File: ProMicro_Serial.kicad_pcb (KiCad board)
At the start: 2 copper layers, 17.8 x 33 mm, 41 parts, among them J1 USB_C_Receptacle_USB2.0, J2 Conn_01x06, U1 FT232H

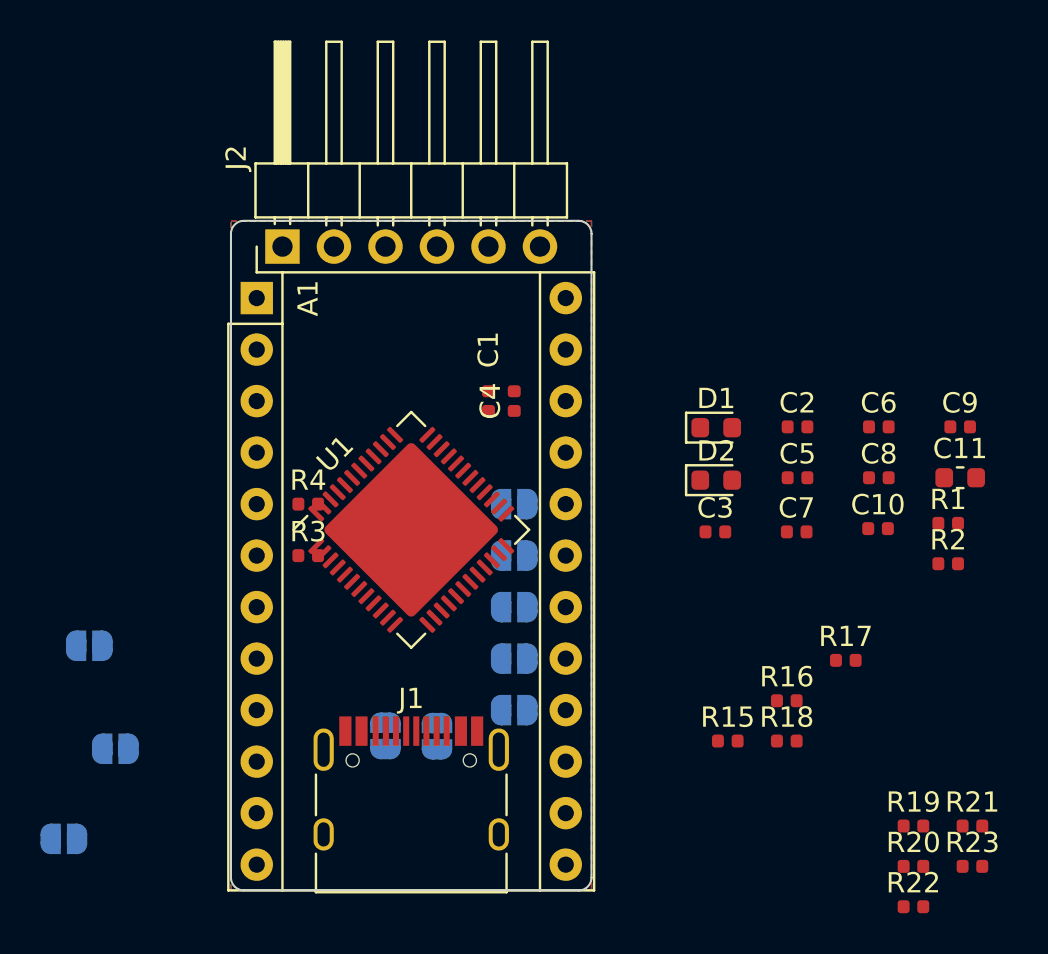
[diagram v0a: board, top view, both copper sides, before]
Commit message: schematic, placed parts
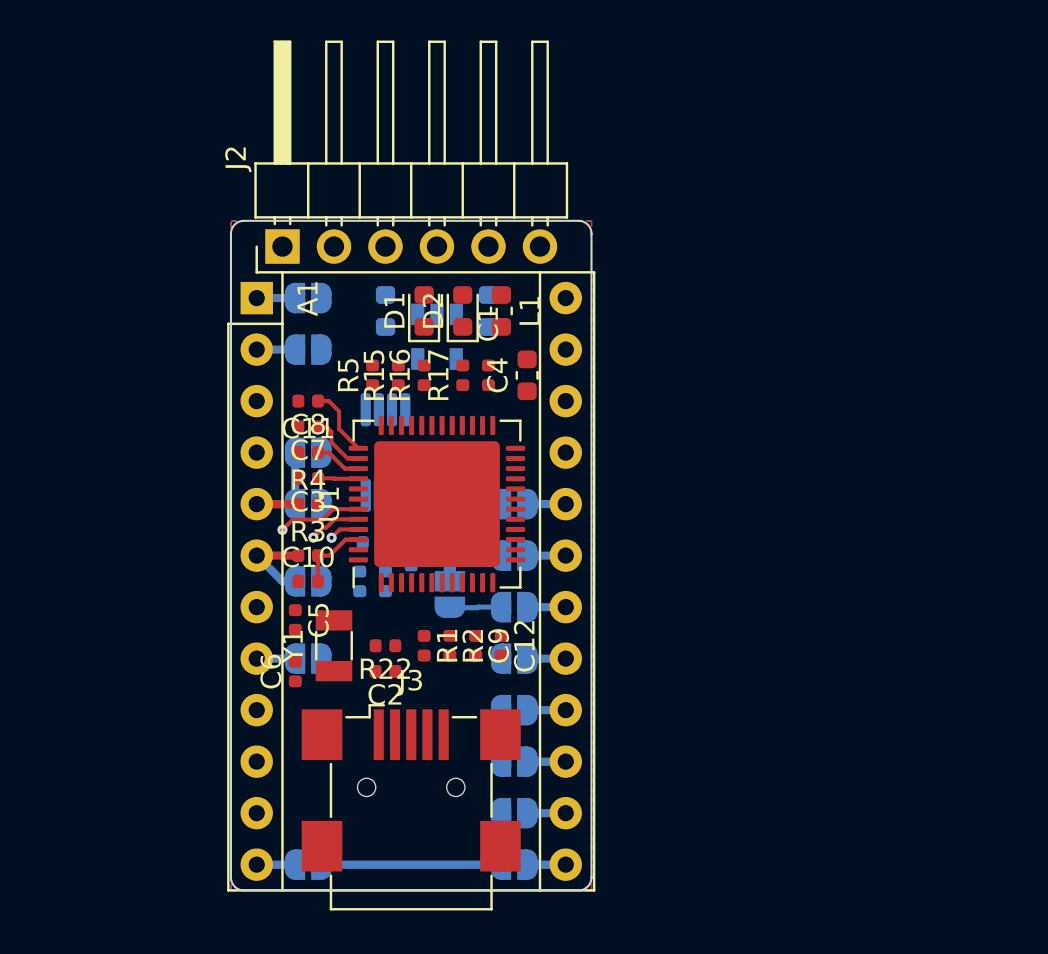
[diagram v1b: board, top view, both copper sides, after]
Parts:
- removed J1: USB_C_Receptacle_USB2.0, Connector_USB:USB_C_Receptacle_HRO_TYPE-C-31-M-12
- removed R18: 4k7, Resistor_SMD:R_0402_1005Metric
- added C12: 100n, Capacitor_SMD:C_0402_1005Metric, F.Cu at (113.7, 93.3)
- added C13: 1µ, Capacitor_SMD:C_0603_1608Metric, B.Cu at (113.0, 76.8)
- added C14: 100n, Capacitor_SMD:C_0603_1608Metric, B.Cu at (108.0, 76.8)
- added J3: USB_B_Mini, Connector_USB:USB_Mini-B_Wuerth_65100516121_Horizontal, F.Cu at (109.2, 100.3)
- added JP11: Jumper_NO_Small, Jumper:SolderJumper-2_P1.3mm_Open_RoundedPad1.0x1.5mm, B.Cu at (104.1, 78.7)
- added JP12: Jumper_NO_Small, Jumper:SolderJumper-2_P1.3mm_Open_RoundedPad1.0x1.5mm, B.Cu at (104.1, 94.0)
- added JP13: Jumper_NO_Small, Jumper:SolderJumper-2_P1.3mm_Open_RoundedPad1.0x1.5mm, B.Cu at (104.1, 83.8)
- added JP14: Jumper_NO_Small, Jumper:SolderJumper-2_P1.3mm_Open_RoundedPad1.0x1.5mm, B.Cu at (104.1, 86.4)
- added JP15: Jumper_NO_Small, Jumper:SolderJumper-2_P1.3mm_Open_RoundedPad1.0x1.5mm, B.Cu at (104.1, 90.2)
- added JP16: Jumper_3_Bridged12, Jumper:SolderJumper-3_P1.3mm_Bridged12_RoundedPad1.0x1.5mm, B.Cu at (111.1, 90.2)
- added L1: 0, Inductor_SMD:L_0603_1608Metric, F.Cu at (113.7, 76.8)
- added R5: 1k, Resistor_SMD:R_0402_1005Metric, F.Cu at (107.3, 80.0)
- added U2: 93CxxB, Package_SO:MSOP-8_3x3mm_P0.65mm, B.Cu at (108.0, 83.8)
- added U3: AZ1117-3.3, Package_TO_SOT_SMD:SOT-23-5, B.Cu at (110.5, 78.1)
- added Y1: 12Mhz, Crystal:Crystal_SMD_3215-2Pin_3.2x1.5mm, F.Cu at (105.4, 93.3)
- C11: footprint Capacitor_SMD:C_0603_1608Metric -> Capacitor_SMD:C_0402_1005Metric
- C4: footprint Capacitor_SMD:C_0402_1005Metric -> Capacitor_SMD:C_0603_1608Metric
- LOGO1: footprint Symbol:OSHW-Logo_7.5x8mm_SilkScreen -> Symbol:OSHW-Logo_5.7x6mm_SilkScreen
- R19, R20, R21: moved to B.Cu
- R23: value 2.2k -> 2k; moved to B.Cu
- moved R23 33.6 mm to (107.3, 88.3), turned to 180 degrees
- moved R21 32.5 mm to (106.7, 90.2), turned to 270 degrees
- moved C11 32.2 mm to (104.1, 83.8)
- moved C6 31.2 mm to (103.5, 94.6), turned to 90 degrees
- moved R20 29.6 mm to (108.0, 90.2), turned to 270 degrees
- moved R22 29.0 mm to (108.0, 93.3), turned to 180 degrees
- moved C8 28.4 mm to (104.1, 81.3), turned to 180 degrees
- moved C10 28.2 mm to (104.1, 90.2)
- moved R19 28.1 mm to (109.2, 88.9), turned to 270 degrees
- moved R1 26.5 mm to (109.9, 93.3), turned to 270 degrees
- moved C9 26.2 mm to (112.4, 93.3), turned to 270 degrees
- moved C5 25.7 mm to (103.5, 92.1), turned to 270 degrees
- moved R2 24.9 mm to (111.1, 93.3), turned to 270 degrees
- moved C7 24.6 mm to (104.1, 82.5), turned to 180 degrees
- moved R15 24.3 mm to (108.6, 80.0), turned to 90 degrees
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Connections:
- net ACBUS7 renamed PWRSAV
- net SCL renamed D3
- net SDA renamed D2
- A1 pad 1: ADBUS0 -> D1
- A1 pad 12: (no net) -> D9
- A1 pad 13: (no net) -> D10
- A1 pad 14: MOSI -> D16
- A1 pad 15: MISO -> D14
- A1 pad 16: SCK -> D15
- A1 pad 17: TDI -> A0
- A1 pad 18: TDO -> A1
- A1 pad 19: TMS -> A2
- A1 pad 2: ADBUS1 -> D0
- A1 pad 20: TCK -> A3
- A1 pad 22: (no net) -> ACBUS0
- A1 pad 24: (no net) -> +5V
- A1 pad 8: (no net) -> D5
- D1 pad 1: ACBUS4 -> Net-(D1-Pad1)
- D1 pad 2: Net-(D1-Pad2) -> +3V3
- D2 pad 1: ACBUS3 -> Net-(D2-Pad1)
- D2 pad 2: Net-(D2-Pad2) -> +3V3
- J2 pad 2: (no net) -> Net-(J2-Pad2)
- J2 pad 6: (no net) -> ADBUS4
- JP1 pad 1: (no net) -> ADBUS0
- JP1 pad 2: ADBUS0 -> D15
- JP10 pad 1: TCK -> ADBUS0
- JP10 pad 2: ADBUS0 -> D1
- JP2 pad 1: (no net) -> ADBUS1
- JP2 pad 2: ADBUS1 -> D16
- JP3 pad 1: SCK -> ADBUS2
- JP3 pad 2: ADBUS0 -> D14
- JP4 pad 1: MOSI -> ADBUS3
- JP4 pad 2: ADBUS1 -> D9
- JP5 pad 1: MISO -> ADBUS3
- JP5 pad 2: ADBUS2 -> D10
- JP6 pad 1: (no net) -> ADBUS0
- JP6 pad 2: ADBUS3 -> A3
- JP7 pad 1: TDI -> ADBUS1
- JP7 pad 2: ADBUS2 -> A0
- JP8 pad 1: TDO -> ADBUS2
- JP8 pad 2: ADBUS1 -> A1
- JP9 pad 1: TMS -> ADBUS3
- JP9 pad 2: ADBUS3 -> A2
- R15 pad 2: (no net) -> +5V
- R16 pad 1: Net-(D1-Pad2) -> TXLED
- R16 pad 2: +3V3 -> Net-(D1-Pad1)
- R17 pad 1: Net-(D2-Pad2) -> RXLED
- R17 pad 2: +3V3 -> Net-(D2-Pad1)
- U1 pad 17: (no net) -> ADBUS4
- U1 pad 21: (no net) -> ACBUS0
- U1 pad 27: ACBUS3 -> RXLED
- U1 pad 28: ACBUS4 -> TXLED
- U1 pad 34: (no net) -> Net-(R5-Pad1)
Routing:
- net ADBUS3: track 0.00 -> 11.4 mm
- net D2: track 0.00 -> 6.50 mm
- net +3V3: track 0.00 -> 5.88 mm
- net D3: track 0.00 -> 4.47 mm
- net /EEDAT: track 0.00 -> 4.17 mm, vias 0 -> 1
- net Net-(C8-Pad1): track 0.00 -> 3.44 mm
- net Net-(C7-Pad1): track 0.00 -> 2.94 mm
- net /EECLK: track 0.00 -> 2.59 mm, vias 0 -> 1
- net ADBUS2: track 0.00 -> 2.54 mm
- net Net-(C2-Pad1): track 0.00 -> 1.98 mm
- net A1: track 0.00 -> 1.91 mm
- net D9: track 0.00 -> 1.89 mm
- net D5: track 0.00 -> 1.89 mm
- net D16: track 0.00 -> 1.89 mm
- net D15: track 0.00 -> 1.89 mm
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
